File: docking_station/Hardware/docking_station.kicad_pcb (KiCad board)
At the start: 2 copper layers, 76 parts, among them IC1 VOM1271T, IC2 VOM1271T, IC3 VOM1271T, IC4 VOM1271T, IC5 VOM1271T, J2 XT60, J3 Conn_01x05_Pin, K1 RELPOL R40N-3021-85-1024, Q1 SIDR392DP-T1-GE3, Q10 DN2540N8-G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

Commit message: trochę zmian fpt
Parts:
- added F1: Fuse, firo_footprints:firo_fuse, F.Cu at (123.2, 127.5)
- added TP23: TestPoint, TestPoint:TestPoint_Bridge_Pitch3.81mm_Drill1.3mm, F.Cu at (111.3, 132.8)
- added TP26: TestPoint, TestPoint:TestPoint_Bridge_Pitch3.81mm_Drill1.3mm, F.Cu at (111.3, 137.5)
- moved K1 82.8 mm to (84.5, 68.9)
- moved Q10 20.0 mm to (122.4, 85.6), turned to 0 degrees
- moved Q11 18.8 mm to (122.4, 91.8), turned to 0 degrees
- moved U3 7.70 mm to (122.4, 97.9)
- moved C9 6.80 mm to (94.2, 106.2)
- moved D1 6.80 mm to (79.5, 104.4)
- moved IC1 6.80 mm to (67.7, 85.4)
- moved IC2 6.80 mm to (67.7, 91.1)
- moved IC3 6.80 mm to (67.7, 96.8)
- moved Q12 6.80 mm to (79.5, 109.0)
- moved Q3 6.80 mm to (102.9, 68.2)
- moved Q9 6.80 mm to (120.0, 68.2)
- moved RV1 6.80 mm to (108.7, 108.5)
- moved TP13 6.80 mm to (100.1, 92.7)
- moved TP14 6.80 mm to (100.1, 96.7)
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
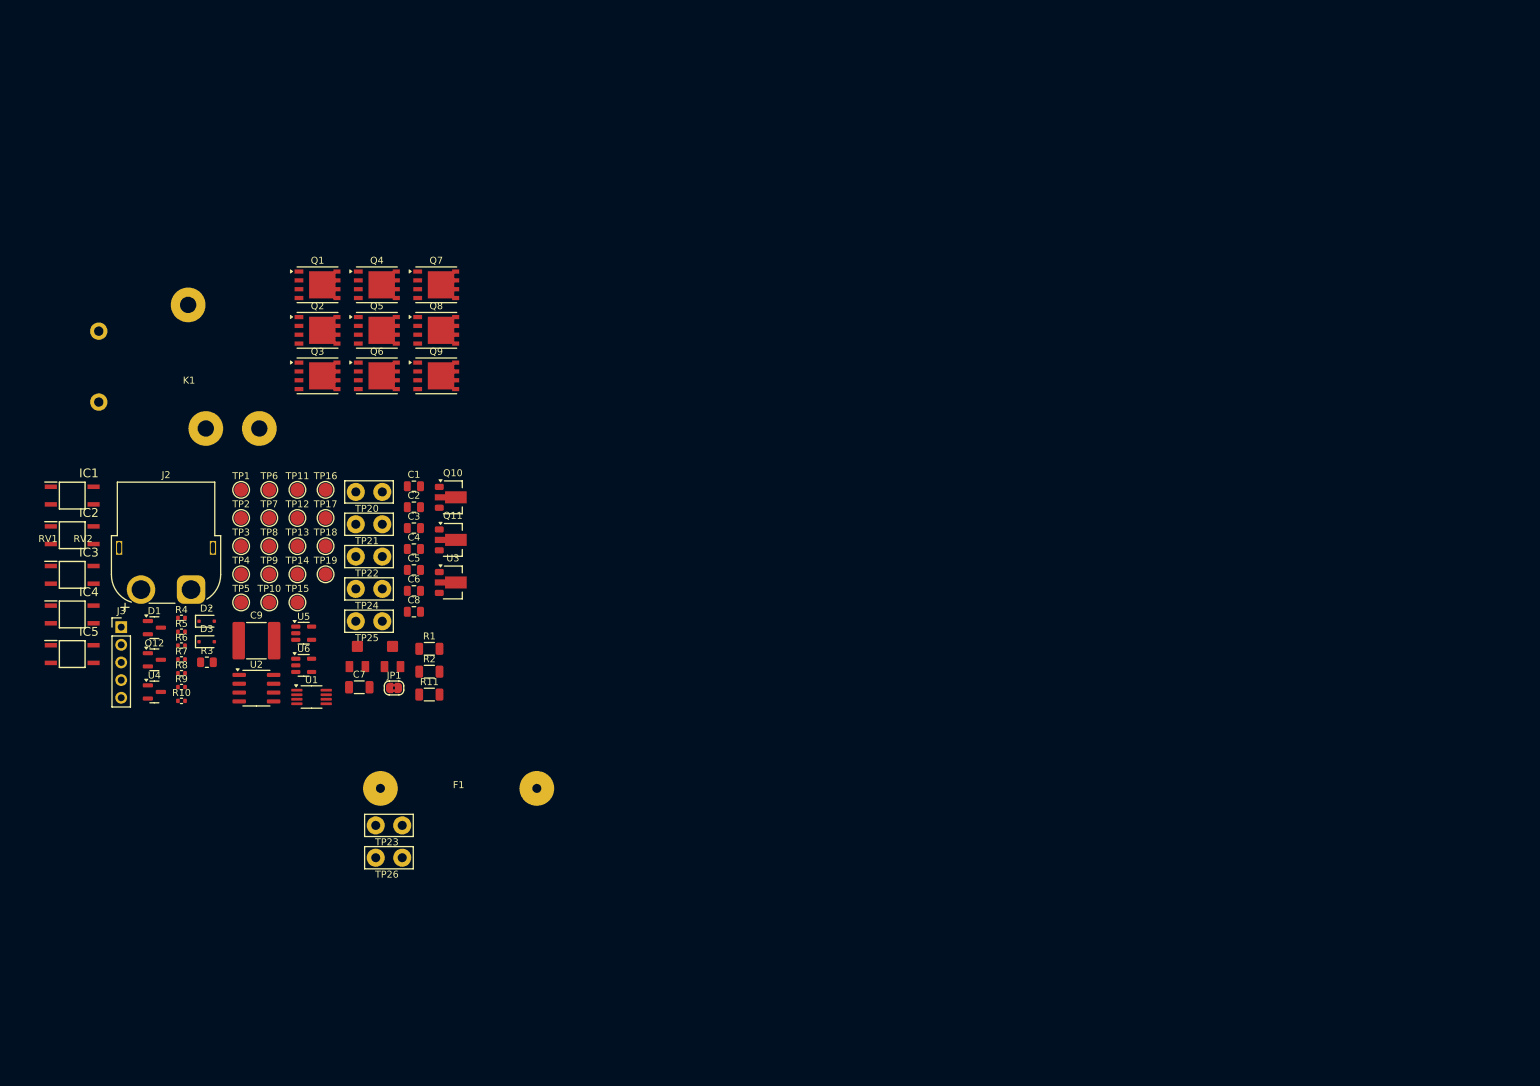
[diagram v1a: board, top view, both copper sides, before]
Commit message: introductory compontent layout
grouped the components, prepped the group layout. The board does seem doable
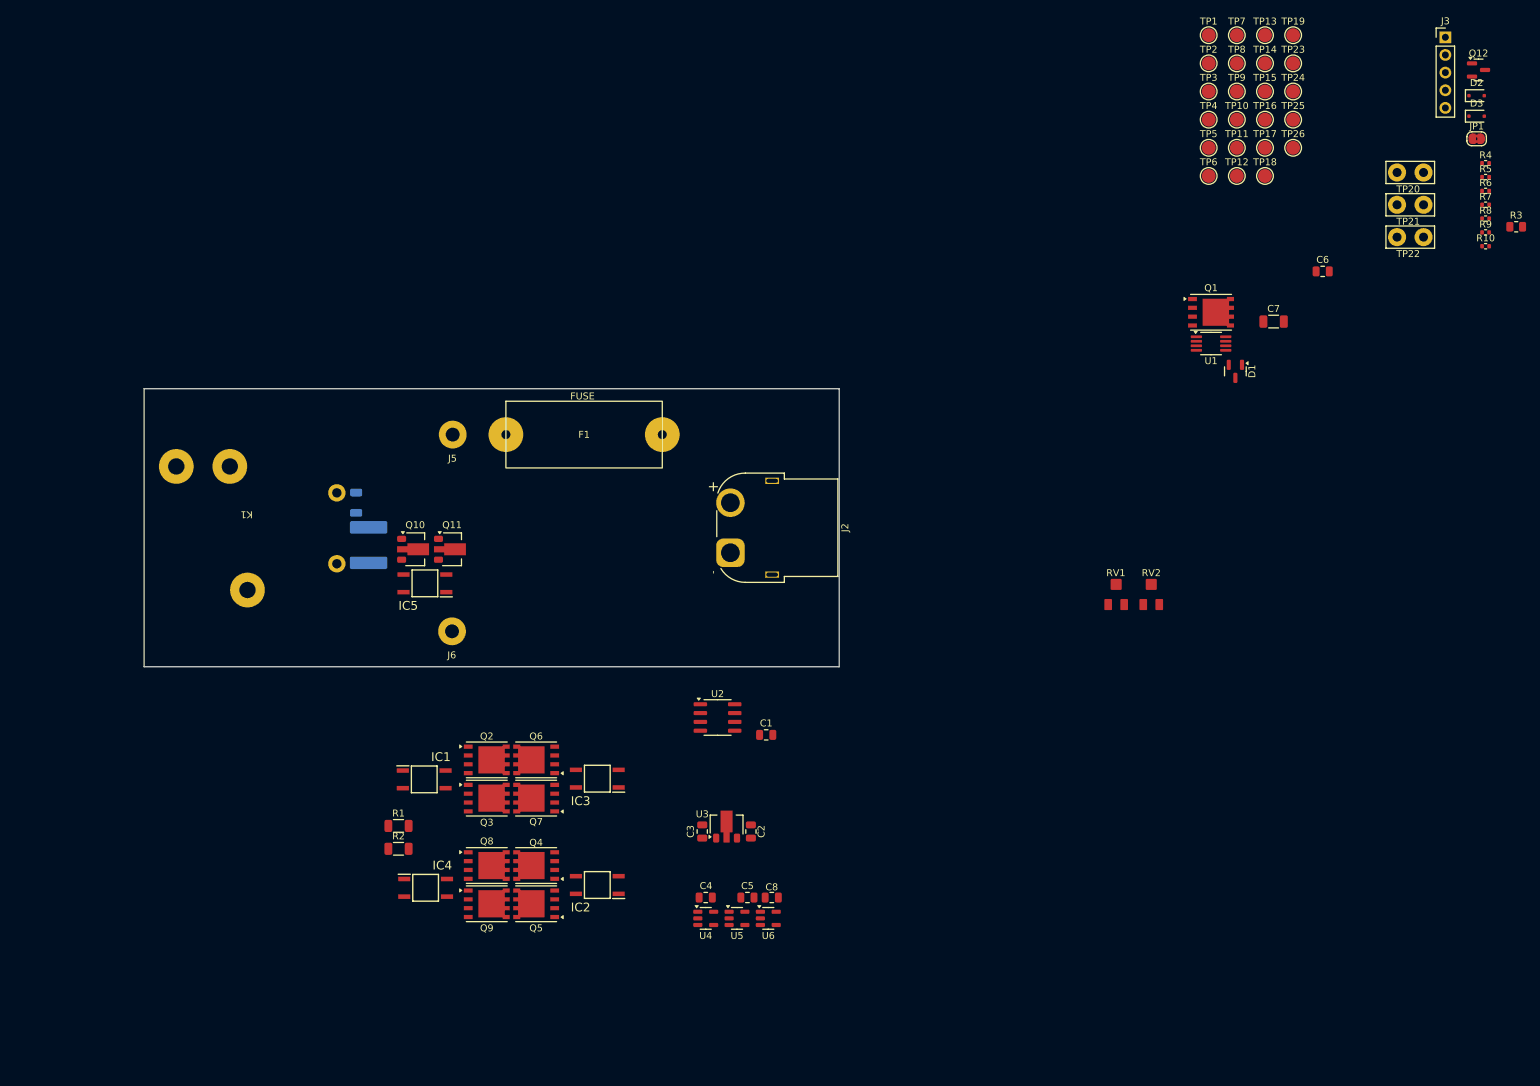
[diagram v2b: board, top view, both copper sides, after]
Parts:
- added J5: SUPPLY+, firo_footprints:14 AWG soldering pad, F.Cu at (122.4, 76.6)
- added J6: SUPPLY-, firo_footprints:14 AWG soldering pad, F.Cu at (122.3, 104.9)
- C9, R11: moved to B.Cu
- Q1, Q2, Q3, Q4, Q5, Q6, Q7, Q8, Q9: footprint Package_SO:PowerPAK_SO-8_Single -> firo_footprints:PowerPAK_SO-8DC for VISHAY SIDR392DP-T1-GE3
- TP23, TP24, TP25, TP26: footprint TestPoint:TestPoint_Bridge_Pitch3.81mm_Drill1.3mm -> TestPoint:TestPoint_Pad_D2.0mm
- U4: footprint Package_TO_SOT_SMD:SOT-23 -> Package_TO_SOT_SMD:SOT-23-5
- moved J3 208.5 mm to (265.2, 19.4)
- moved Q12 208.5 mm to (270.0, 24.1)
- moved R10 198.7 mm to (271.0, 49.5)
- moved R4 198.7 mm to (271.0, 37.6)
- moved R5 198.7 mm to (271.0, 39.5)
- moved R6 198.7 mm to (271.0, 41.5)
- moved R7 198.7 mm to (271.0, 43.5)
- moved R8 198.7 mm to (271.0, 45.5)
- moved R9 198.7 mm to (271.0, 47.5)
- moved R3 198.5 mm to (275.4, 46.7)
- moved D3 197.7 mm to (269.7, 30.8)
- moved D2 197.7 mm to (269.7, 27.8)
- moved JP1 174.6 mm to (269.7, 34.0)
- moved TP23 171.6 mm to (243.3, 23.2)
- moved TP26 166.9 mm to (243.3, 35.3)
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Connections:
- U4 pad 2: Net-(U4--) -> GND
- U4 pad 3: +5V -> Net-(U4--)
- U5 pad 1: /AMP_OUT -> Net-(R7-Pad2)
- U5 pad 4: Net-(R7-Pad2) -> /AMP_OUT
- U6 pad 1: Net-(U6--) -> Net-(JP1-A)
- U6 pad 4: Net-(JP1-A) -> Net-(U6--)
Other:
- board outline added: 100 x 40 mm

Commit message: big layout progress
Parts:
- added J4: SUPPLY+, firo_footprints:14 AWG soldering pad, F.Cu at (153.4, 58.8)
- added J7: SUPPLY-, firo_footprints:14 AWG soldering pad, F.Cu at (162.0, 76.6)
- D1, IC1, IC2, Q1, U1, U2: moved to B.Cu
- moved R3 224.3 mm to (68.2, 132.6)
- moved Q12 224.0 mm to (74.0, 132.7)
- moved D1 98.8 mm to (136.4, 73.1), turned to 0 degrees
- moved U1 96.7 mm to (137.3, 85.5)
- moved Q1 96.2 mm to (140.4, 90.0)
- moved IC3 73.2 mm to (80.8, 164.3), turned to 90 degrees
- moved Q5 69.6 mm to (155.3, 77.7), turned to 90 degrees
- moved J3 67.1 mm to (239.5, 81.4)
- moved IC2 62.8 mm to (162.5, 81.6)
- moved IC5 62.6 mm to (64.2, 129.3)
- moved Q10 62.6 mm to (62.8, 124.4)
- moved Q11 62.6 mm to (68.1, 124.4)
- moved Q4 57.2 mm to (155.3, 85.3), turned to -90 degrees
- moved C6 55.8 mm to (226.3, 104.7), turned to 180 degrees
- moved C4 55.4 mm to (207.8, 117.3)
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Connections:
- net Net-(IC1-K_2) renamed /CS_1
- net Net-(IC2-K_2) renamed /CS_2
- net Net-(IC3-K_2) renamed /CS_3
- net Net-(IC4-K_2) renamed /CS_4
- Q2 pad 3: VDC -> +24V
- Q6 pad 3: VDC -> +24V
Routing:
- net Net-(Q1-G): track 0.00 -> 5.52 mm
- added copper zone on B.Cu, net +24V
- added copper zone on F.Cu, net +24V
- added copper zone on F.Cu, net /CS_1
- added copper zone on F.Cu, net /CS_2
- added copper zone on F.Cu, net /CS_3
- added copper zone on F.Cu, net /CS_4
- added copper zone on F.Cu, net /LINE_A
- added copper zone on F.Cu, net /LINE_B
- added copper zone on B.Cu, net GND
- added copper zone on B.Cu, net SENSE-

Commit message: work still in progress
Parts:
- C1, C2, C3, IC3, IC4, Q10, Q11, Q12, R1, R10, R2, R4, R5, R7, U3: moved to B.Cu
- D1: moved to F.Cu
- moved R4 161.6 mm to (115.2, 80.6), turned to 90 degrees
- moved R5 160.1 mm to (116.2, 80.6), turned to 90 degrees
- moved R6 159.5 mm to (117.5, 84.9), turned to -90 degrees
- moved R7 155.1 mm to (119.7, 77.5), turned to 180 degrees
- moved R9 153.6 mm to (122.0, 84.9), turned to -90 degrees
- moved R10 151.6 mm to (122.1, 77.9), turned to 90 degrees
- moved JP1 151.0 mm to (126.6, 82.2), turned to -90 degrees
- moved R8 142.4 mm to (131.8, 75.6), turned to -90 degrees
- moved D3 125.8 mm to (164.4, 99.7)
- moved D2 117.6 mm to (164.5, 80.4)
- moved J3 116.8 mm to (122.9, 88.2)
- moved C7 111.5 mm to (130.1, 75.7), turned to -90 degrees
- moved RV2 104.0 mm to (123.2, 81.7)
- moved C4 103.0 mm to (114.2, 74.5)
- moved C5 103.0 mm to (120.2, 74.5)
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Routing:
- net /LINE_B: track 0.00 -> 64.9 mm, vias 0 -> 1
- net /LINE_A: track 0.00 -> 57.9 mm, vias 0 -> 1
- net +5V: track 0.00 -> 40.1 mm
- net CH_END: track 0.00 -> 22.1 mm
- net Net-(IC3-A_2): track 0.00 -> 18.7 mm, vias 0 -> 2
- net Net-(IC1-A_2): track 0.00 -> 15.4 mm, vias 0 -> 2
- net Net-(IC5-A_2): track 0.00 -> 12.5 mm, vias 0 -> 1
- net /CS_3: track 0.00 -> 12.4 mm, vias 0 -> 1
- net Net-(Q10-D): track 0.00 -> 11.5 mm
- net Net-(JP1-A): track 0.00 -> 11.1 mm, vias 0 -> 1
- net Net-(IC2-A_2): track 0.00 -> 10.0 mm, vias 0 -> 2
- net Net-(IC4-A_2): track 0.00 -> 9.76 mm, vias 0 -> 2
- net Net-(IC5-K_2): track 0.00 -> 8.50 mm, vias 0 -> 1
- net /AMP_OUT: track 0.00 -> 8.25 mm, vias 0 -> 2
- net /CS_1: track 0.00 -> 8.18 mm, vias 0 -> 1
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- added copper zone on B.Cu, net SENSE+
- added copper zone on F.Cu, net SENSE+
- added copper zone on F.Cu, net SENSE-

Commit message: yee
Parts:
- removed TP6: TestPoint, TestPoint:TestPoint_Pad_D2.0mm
- added H1: MountingHole_Pad, MountingHole:MountingHole_3.2mm_M3_Pad_Via, F.Cu at (69.5, 105.5)
- added H2: MountingHole_Pad, MountingHole:MountingHole_3.2mm_M3_Pad_Via, F.Cu at (172.0, 105.0)
- added H3: MountingHole_Pad, MountingHole:MountingHole_3.2mm_M3_Pad_Via, F.Cu at (172.1, 76.3)
- added H4: MountingHole_Pad, MountingHole:MountingHole_3.2mm_M3_Pad_Via, F.Cu at (69.5, 75.0)
- C4, C5, C6, C8, R6, R9, U4: moved to B.Cu
- R7: moved to F.Cu
- moved C6 96.5 mm to (130.3, 94.6), turned to -90 degrees
- moved U4 16.6 mm to (127.2, 87.8), turned to 90 degrees
- moved C4 16.3 mm to (127.2, 84.3), turned to 90 degrees
- moved R4 14.5 mm to (126.0, 90.3), turned to 0 degrees
- moved R5 11.8 mm to (125.0, 88.4)
- moved C5 10.9 mm to (124.9, 84.3), turned to 90 degrees
- moved J5 10.5 mm to (124.0, 107.0)
- moved R8 9.61 mm to (123.8, 81.0), turned to 180 degrees
- moved R9 9.55 mm to (126.2, 76.3), turned to 180 degrees
- moved U5 8.84 mm to (124.3, 84.3), turned to -90 degrees
- moved JP1 7.60 mm to (119.8, 78.8)
- moved C7 7.59 mm to (123.5, 79.3), turned to 180 degrees
- moved R7 6.88 mm to (125.3, 81.5), turned to -90 degrees
- moved RV2 6.76 mm to (127.8, 76.8)
- moved R6 5.47 mm to (122.9, 85.8), turned to 0 degrees
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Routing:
- net +5V: track 40.1 -> 27.5 mm, vias 0 -> 2
- net /AMP_OUT: track 8.25 -> 14.8 mm, vias 2 -> 1
- net GND: track 6.33 -> 0.00 mm, vias 1 -> 0
- net /CS_VOUT: track 7.83 -> 2.25 mm
- net Net-(R6-Pad1): track 1.26 -> 5.08 mm, vias 0 -> 1
- net Net-(JP1-A): track 11.1 -> 7.42 mm
- net Net-(U6--): track 4.46 -> 7.48 mm
- net Net-(IC5-A_1): track 0.00 -> 2.66 mm
- net Net-(U6-+): track 4.32 -> 6.64 mm, vias 1 -> 0
- net Net-(R9-Pad1): track 1.26 -> 2.73 mm, vias 0 -> 1
- net Net-(R7-Pad2): track 2.28 -> 1.18 mm, vias 1 -> 0
- net Net-(U4--): track 3.60 -> 2.93 mm, vias 1 -> 0
- net Net-(IC4-A_2): track 9.76 -> 10.4 mm
- net Net-(IC1-A_2): track 15.4 -> 14.8 mm
- net CH_END: track 22.1 -> 22.5 mm, vias 0 -> 1
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- added copper zone on F.Cu, net GND
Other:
- board size 100 x 40 mm -> 114.5 x 41 mm

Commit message: almost finished
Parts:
- removed J4: SUPPLY+, firo_footprints:14 AWG soldering pad
- removed J7: SUPPLY-, firo_footprints:14 AWG soldering pad
- removed TP11, TP12, TP13, TP14, TP15, TP16, TP17, TP18, TP19, TP23, TP24, TP25, TP26: TestPoint, TestPoint:TestPoint_Pad_D2.0mm
- added CG1: TestPoint, TestPoint:TestPoint_Pad_D2.0mm, F.Cu at (138.5, 104.4)
- added CG2: TestPoint, TestPoint:TestPoint_Pad_D2.0mm, B.Cu at (158.4, 77.7)
- added CG3: TestPoint, TestPoint:TestPoint_Pad_D2.0mm, F.Cu at (134.8, 81.0)
- added CG4: TestPoint, TestPoint:TestPoint_Pad_D2.0mm, F.Cu at (160.0, 97.4)
- added CS1: TestPoint, TestPoint:TestPoint_Pad_D2.0mm, F.Cu at (138.5, 99.0)
- added CS2: TestPoint, TestPoint:TestPoint_Pad_D2.0mm, B.Cu at (158.0, 85.1)
- added CS3: TestPoint, TestPoint:TestPoint_Pad_D2.0mm, F.Cu at (138.0, 81.0)
- added CS4: TestPoint, TestPoint:TestPoint_Pad_D2.0mm, F.Cu at (160.0, 100.8)
- added H5: MountingHole_Pad, MountingHole:MountingHole_2.2mm_M2_Pad_Via, F.Cu at (75.6, 76.6)
- added H6: MountingHole_Pad, MountingHole:MountingHole_2.2mm_M2_Pad_Via, F.Cu at (101.8, 106.4)
- added H7: MountingHole_Pad, MountingHole:MountingHole_2.2mm_M2_Pad_Via, F.Cu at (97.6, 76.6)
- added TP6: TestPoint, TestPoint:TestPoint_Pad_D2.0mm, B.Cu at (122.3, 83.5)
- TP4, TP5: moved to B.Cu
- moved TP9 149.1 mm to (107.6, 104.3), turned to 180 degrees
- moved TP10 136.1 mm to (107.6, 78.5)
- moved TP1 136.0 mm to (124.1, 103.0)
- moved TP8 127.3 mm to (119.1, 75.4)
- moved TP7 123.2 mm to (128.4, 80.6)
- moved TP3 114.7 mm to (138.1, 94.3)
- moved GND3 110.6 mm to (165.1, 107.8), turned to 90 degrees
- moved TP2 104.3 mm to (142.9, 78.7)
- moved TP4 100.3 mm to (152.3, 93.3), turned to 180 degrees
- moved TP5 94.2 mm to (152.3, 86.8), turned to 180 degrees
- moved GND2 91.6 mm to (107.8, 73.3)
- moved GND1 48.5 mm to (166.0, 75.5), turned to 180 degrees
- moved J6 1.58 mm to (160.5, 105.0)
- renumbered TP20 to GND1, TP21 to GND2, TP22 to GND3
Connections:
- TP1 pad 1: +24V -> Net-(J4-Pin_1)
- TP10 pad 1: Net-(Q10-D) -> /LINE_B
- TP2 pad 1: +5V -> +24V
- TP3 pad 1: /LINE_A -> +5V
- TP4 pad 1: /LINE_B -> /LINE_A
- TP5 pad 1: /CS_VOUT -> /LINE_B
- TP7 pad 1: Net-(R7-Pad2) -> Net-(U6-+)
- TP8 pad 1: Net-(U6-+) -> Net-(JP1-A)
- TP9 pad 1: Net-(JP1-A) -> Net-(Q10-D)
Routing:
- net Net-(Q10-D): track 11.5 -> 21.4 mm
- net /CS_VOUT: track 2.25 -> 11.8 mm, vias 0 -> 1
- net /LINE_B: track 64.9 -> 72.2 mm, vias 1 -> 2
- net Net-(IC1-A_2): track 14.8 -> 20.6 mm, vias 2 -> 3
- net +5V: track 27.5 -> 33.0 mm, vias 2 -> 3
- net Net-(R7-Pad2): track 1.18 -> 6.45 mm, vias 0 -> 1
- net Net-(J4-Pin_1): track 0.00 -> 4.04 mm
- net /CS_1: track 8.24 -> 12.2 mm, vias 1 -> 2
- net Net-(JP1-A): track 7.42 -> 10.9 mm
- net Net-(IC3-A_2): track 18.7 -> 22.0 mm, vias 2 -> 3
- net Net-(U6-+): track 6.64 -> 9.90 mm
- net /CS_3: track 12.7 -> 15.9 mm, vias 1 -> 2
- net Net-(IC4-A_2): track 10.4 -> 13.0 mm
- net /CS_2: track 2.34 -> 4.94 mm
- net /CS_4: track 2.30 -> 4.71 mm
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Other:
- board text added: "+24V"
- board text added: "+5V"
- board text added: "CHG_TSH"
- board text added: "CH_END"
- board text added: "CUR TSH"
- board text added: "LINE A"
- board text added: "LINE B"
- board text added: "REL A"
- board text added: "REL B"
- board text added: "SUP+"
